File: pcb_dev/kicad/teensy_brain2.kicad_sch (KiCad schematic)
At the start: 55 parts, among them J1 teensy4.1

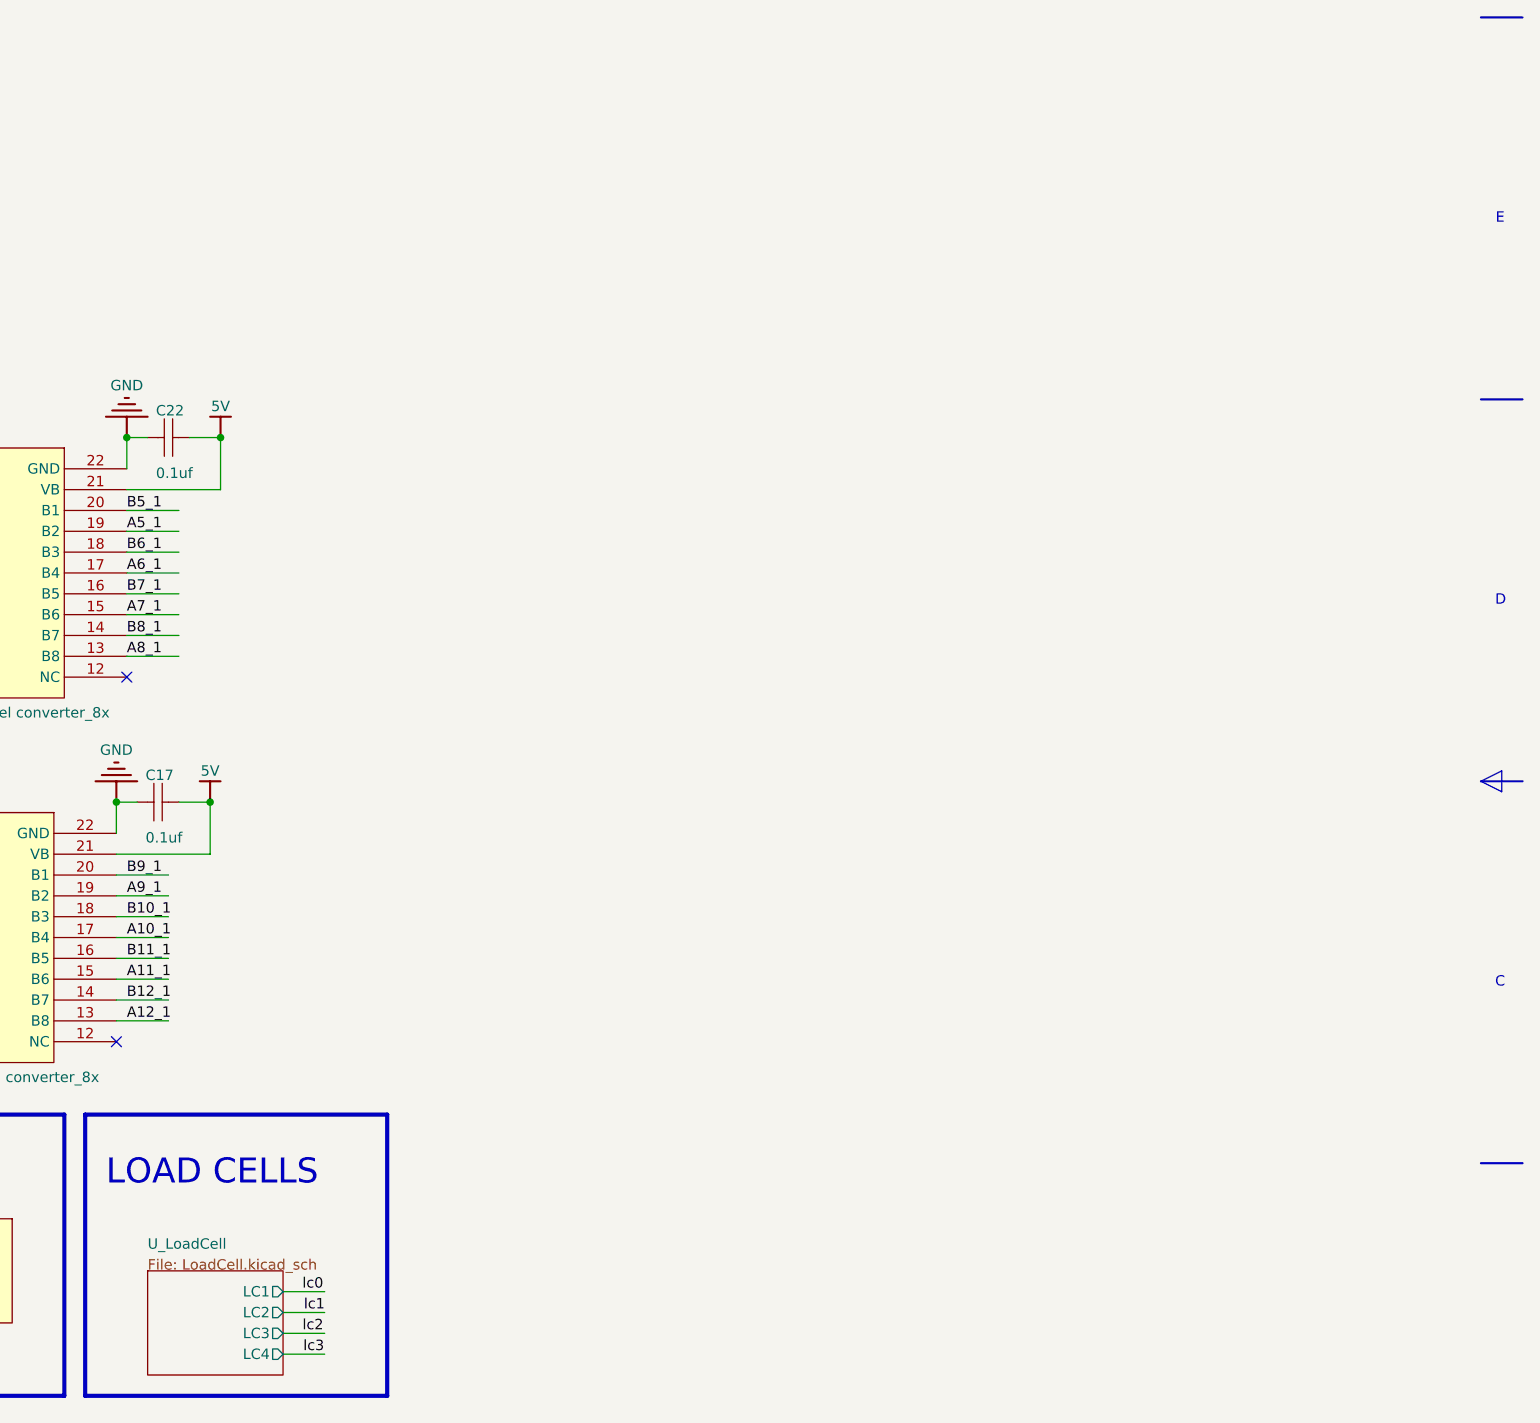
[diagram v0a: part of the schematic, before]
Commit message: removed unneeded drawings
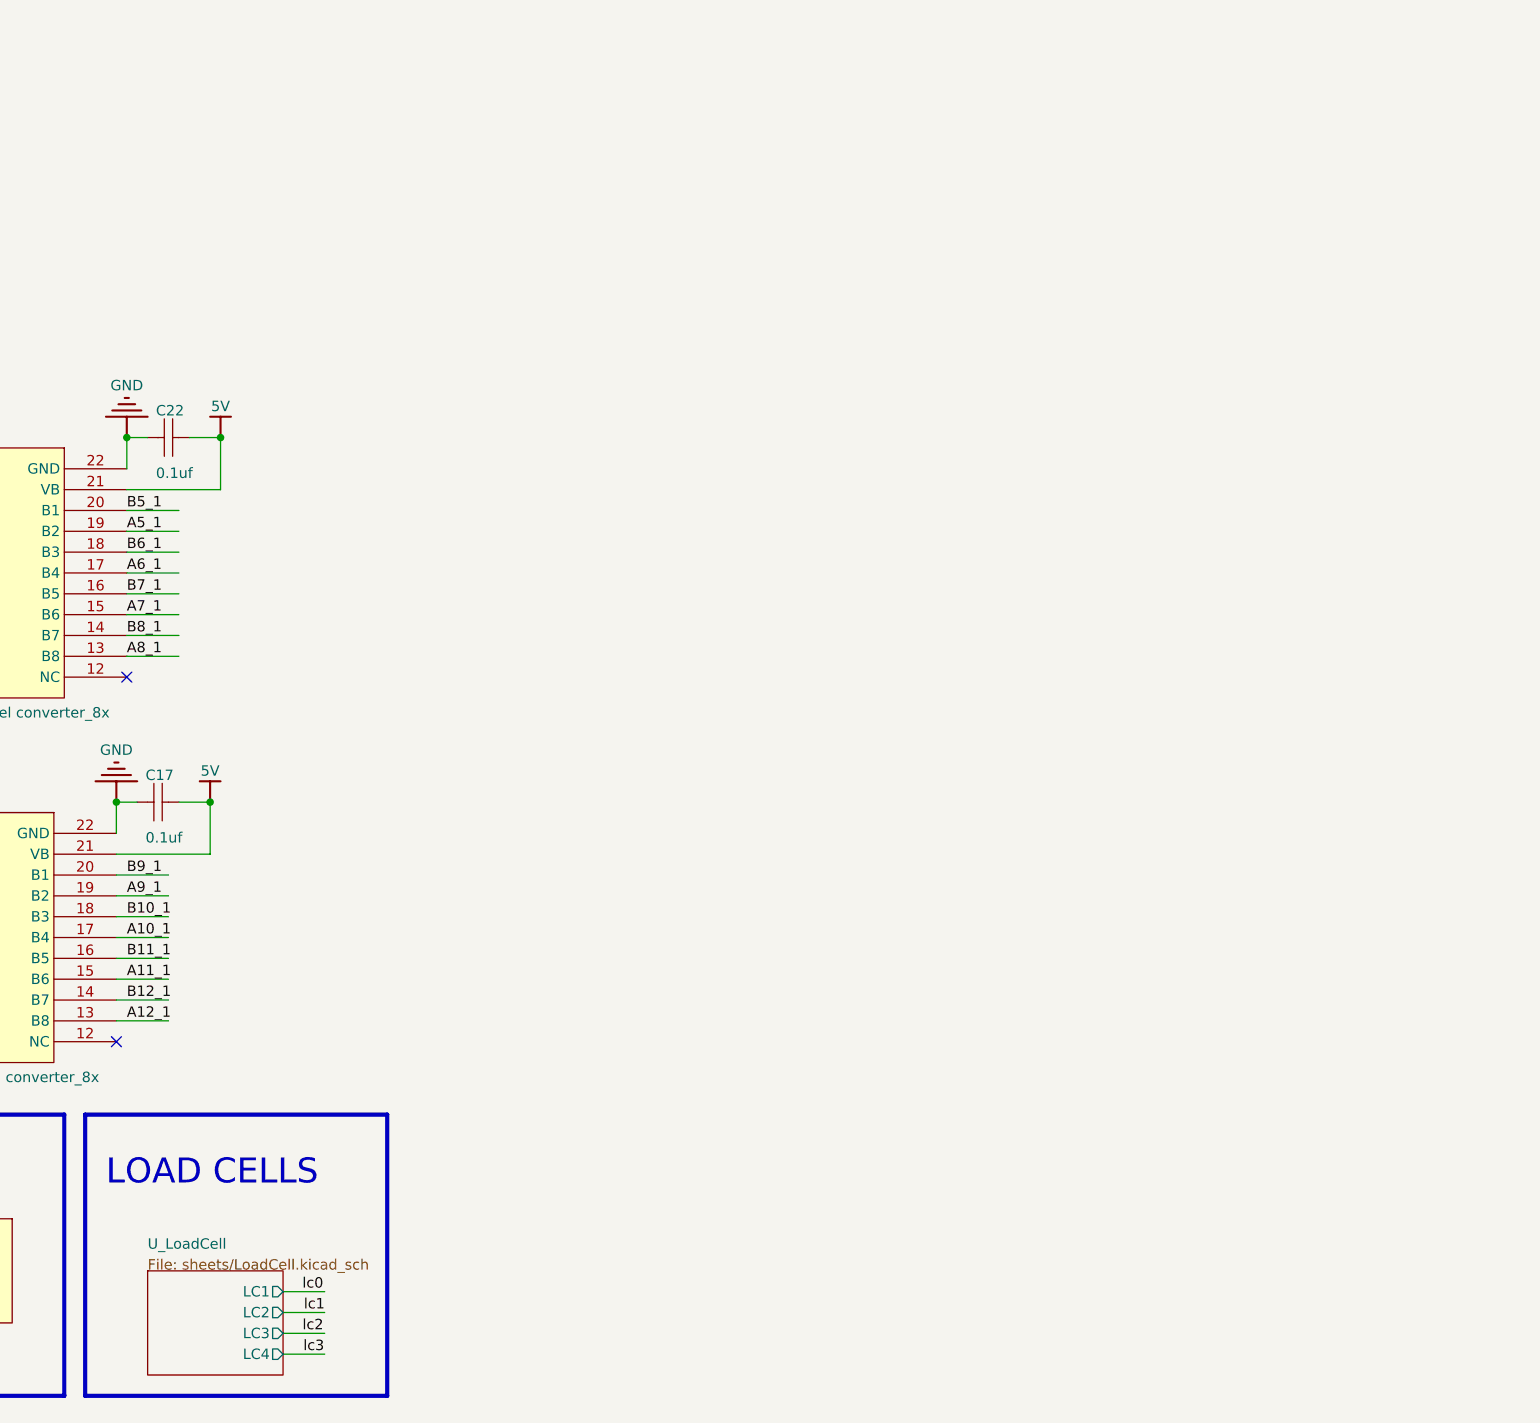
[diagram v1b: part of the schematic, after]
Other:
- sheet U_LoadCell: file LoadCell.kicad_sch -> sheets/LoadCell.kicad_sch
- note removed: "C"
- note removed: "D"
- note removed: "E"
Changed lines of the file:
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@@
 		)
 	)
-	(polyline
-		(pts
-			(xy 426.72 76.2) (xy 429.26 77.47) (xy 429.26 74.93) (xy 426.72 76.2)
-		)
-		(stroke
-			(width 0.0254)
-			(type solid)
-			(color 0 0 0 1)
-		)
-		(fill
-			(type color)
-			(color 0 0 0 1)
-		)
-	)
 	(rectangle
 		(start 212.09 116.84)
@@
 		)
 	)
-	(text "D"
-		(exclude_from_sim no)
-		(at 428.454 54.949 0)
-		(effects
-			(font
-				(size 1.27 1.27)
-			)
-			(justify left bottom)
-		)
-	)
-	(text "E"
-		(exclude_from_sim no)
-		(at 428.518 8.382 0)
-		(effects
-			(font
-				(size 1.27 1.27)
-			)
-			(justify left bottom)
-		)
-	)
 	(text "LOAD CELLS"
 		(exclude_from_sim no)
@@
 		)
 	)
-	(text "C"
-		(exclude_from_sim no)
-		(at 428.454 101.515 0)
-		(effects
-			(font
-				(size 1.27 1.27)
-			)
-			(justify left bottom)
-		)
-	)
 	(text "BATTERY INPUT"
 		(exclude_from_sim no)
@@
 		)
 	)
-	(polyline
-		(pts
-			(xy 426.72 76.2) (xy 431.8 76.2)
-		)
-		(stroke
-			(width 0.254)
-			(type solid)
-			(color 0 0 0 1)
-		)
-	)
 	(wire
 		(pts
@@
 		)
 	)
-	(polyline
-		(pts
-			(xy 426.72 122.767) (xy 431.8 122.767)
-		)
-		(stroke
-			(width 0.254)
-			(type solid)
-			(color 0 0 0 1)
-		)
-	)
 	(wire
 		(pts
@@
 		)
 	)
-	(polyline
-		(pts
-			(xy 426.72 29.633) (xy 431.8 29.633)
-		)
-		(stroke
-			(width 0.254)
-			(type solid)
-			(color 0 0 0 1)
-		)
-	)
 	(wire
 		(pts
@@
 		)
 	)
-	(polyline
-		(pts
-			(xy 426.72 -16.933) (xy 431.8 -16.933)
-		)
-		(stroke
-			(width 0.254)
-			(type solid)
-			(color 0 0 0 1)
-		)
-	)
 	(wire
 		(pts
@@
 			)
 		)
-		(property "Sheetfile" "LoadCell.kicad_sch"
+		(property "Sheetfile" "sheets/LoadCell.kicad_sch"
 			(at 264.16 135.89 0)
 			(effects
